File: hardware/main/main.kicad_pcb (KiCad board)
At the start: 2 copper layers, 68 x 76 mm, 68 parts, among them J1 Conn_01x06, J2 Conn_01x05, J3 Conn_01x01, J4 USB_B_Micro, J5 Conn_01x04, J7 Conn_01x02, J8 Conn_01x02, SW1 PEC12R-4217F-S0024, U1 E73-2G4M08S1C-52840, U10 DCX114YU, U12 NCV7428MW3, U2 MAX98357A, U3 MOC3043M, U4 SP3485, U5 NCV7428MW3, U6 BME680, U7 TPS82130, U8 D203S, U9 UG-2864ASWPG01, Y1 32768Hz

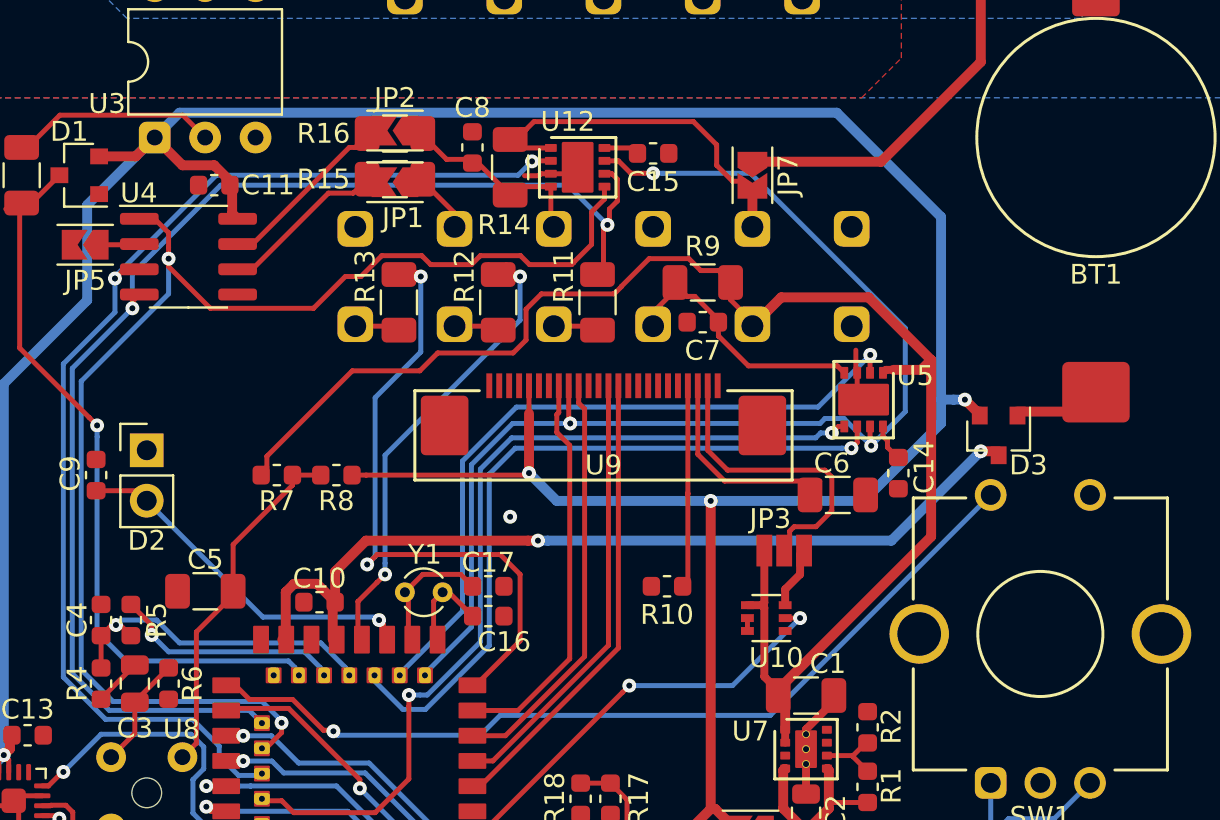
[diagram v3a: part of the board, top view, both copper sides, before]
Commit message: Add indicator LEDs to switch
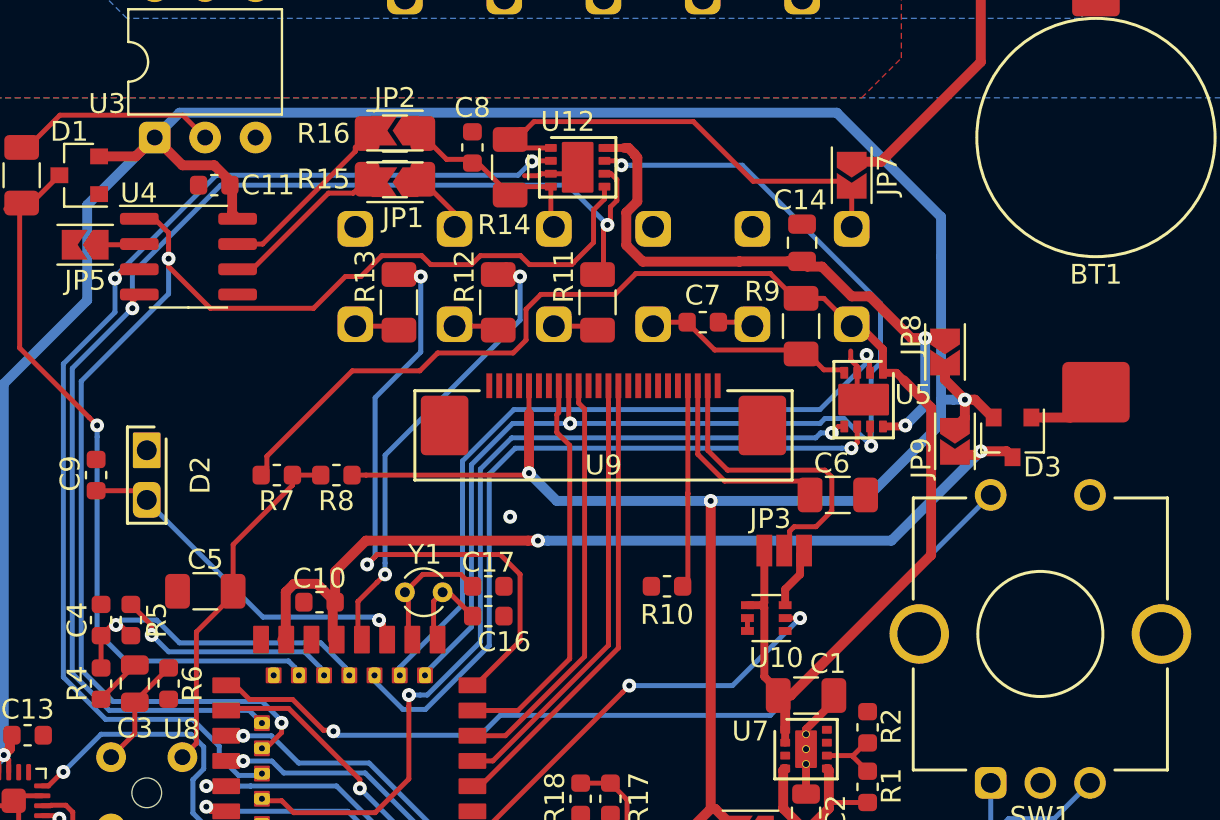
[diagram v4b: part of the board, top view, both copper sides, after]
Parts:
- removed C15: 100n, Capacitor_SMD:C_0603_1608Metric
- added JP8: SolderJumper_2_Open, RoomControl:Jumper2, F.Cu at (117.2, 107.8)
- added JP9: SolderJumper_2_Open, RoomControl:Jumper2, F.Cu at (117.7, 112.3)
- C14: value 100n -> 22u/16V; footprint Capacitor_SMD:C_0603_1608Metric -> Capacitor_SMD:C_0805_2012Metric
- D2: footprint Connector_PinHeader_2.54mm:PinHeader_1x02_P2.54mm_Vertical -> RoomControl:DiodeHoles
- moved C14 12.6 mm to (110.0, 102.3), turned to 270 degrees
- moved R9 5.42 mm to (110.0, 106.5), turned to 90 degrees
- moved JP7 5.00 mm to (112.5, 98.9)
- moved D2 1.25 mm to (77.0, 114.0), turned to 270 degrees
- moved D3 0.71 mm to (120.6, 112.1)
- turned C7 to 0 degrees
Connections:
- J1 pad 5: +12V -> GND
- J1 pad 6: GND -> +12V
- U12 pad 8: Net-(C15-Pad2) -> Net-(C14-Pad2)
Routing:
- net Net-(C14-Pad2): track 1.96 -> 30.5 mm, vias 0 -> 2
- net Net-(JP7-Pad1): track 26.7 -> 21.7 mm
- net +3V3: track 180.4 -> 184.9 mm
- net LIN: track 14.0 -> 11.2 mm
- net Net-(C10-Pad1): track 45.2 -> 47.4 mm
- net GND: track 25.5 -> 27.5 mm
- net Net-(C15-Pad2): track 1.78 -> 0.00 mm
- net +12V: track 96.1 -> 94.8 mm
- net RESET: track 61.4 -> 60.4 mm
- net Net-(BT1-Pad1): track 4.35 -> 3.78 mm
